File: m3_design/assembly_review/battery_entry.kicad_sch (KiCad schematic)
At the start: 28 parts, among them J1 BAT+ / GND / SW / SW, U9 TPS259470LRPWR

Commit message: R10: m3_design/r10_build.sh and per-family stage gate; m3_design/assembly_review rebuilt as M3-ASSY-R10 (board 883d2db5..., 46 x 90 mm); tools/check.sh passes at zero; binding note bound to the board
Co-Authored-By: Claude Opus 5.5 <noreply@anthropic.com>
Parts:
- added J400: BM02B-GHS-TBT(LF)(SN), rocket:M3_GH_BM02B_GHS_TBT, symbol M3:Conn_1x2
- J1: value BAT+ / GND / SW / SW -> DB125-3.5-2P-GN-S; footprint rocket:M3_DB128V_4P_Entry -> rocket:M3_DB125_2P_GN; symbol M3:BatteryTerminal -> M3:Conn_1x2; LCSC C2915641 -> C466970; Manufacturer Part DB128V-5.08-4P-GN-S -> DB125-3.5-2P-GN-S
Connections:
- net BAT_SW_RETURN: now also J400.2; no longer J1.4 (SW RETURN)
- net BAT_SW_SOURCE: now also J400.1; no longer J1.3 (SW SOURCE)
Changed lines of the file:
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@@
 		(title "07 | Battery input, contact and protection")
 		(date "2026-09-07")
-		(rev "M3-ASSY-R9")
+		(rev "M3-ASSY-R10")
 		(company "Single-board M3 candidate; full system incomplete"))
 	(text "07 | Battery input, contact and protection"
@@
 			(font
 				(size 2.54 2.54))
-			(justify left))
-)
-	(symbol
-		(lib_id "M3:BatteryTerminal")
-		(at 71.12 71.12 0)
-		(unit 1)
-		(in_bom yes)
-		(on_board yes)
-		(dnp no)
-		(property "Reference" "J1"
-			(at 71.12 62.23 0)
-			(effects
-				(font
-					(size 1.27 1.27))))
-		(property "Value" "BAT+ / GND / SW / SW"
-			(at 71.12 66.03999999999999 0)
-			(effects
-				(font
-					(size 1.27 1.27))))
-		(property "Footprint" "rocket:M3_DB128V_4P_Entry"
-			(at 71.12 71.12 0)
-			(hide yes)
-			(effects
-				(font
-					(size 1.27 1.27))))
-		(property "Datasheet" ""
-			(at 71.12 71.12 0)
-			(hide yes)
-			(effects
-				(font
-					(size 1.27 1.27))))
-		(property "LCSC" "C2915641"
-			(at 71.12 71.12 0)
-			(hide yes)
-			(effects
-				(font
-					(size 1.27 1.27))))
-		(property "Manufacturer" "DORABO"
-			(at 71.12 71.12 0)
-			(hide yes)
-			(effects
-				(font
-					(size 1.27 1.27))))
-		(property "Manufacturer Part" "DB128V-5.08-4P-GN-S"
-			(at 71.12 71.12 0)
-			(hide yes)
-			(effects
-				(font
-					(size 1.27 1.27))))
-		(instances
-			(project "m3"
-				(path "/6007a7db-6a58-5660-8beb-956dea045ff8/69ee5338-a377-5d7b-bbd8-28b781c5d2c5"
-					(reference "J1")
-					(unit 1)))))
-	(wire
-		(pts
-			(xy 45.72 69.85)
-			(xy 40.64 69.85))
-		(stroke
-			(width 0)
-			(type default))
-)
-	(global_label "BAT_IN"
-		(shape passive)
-		(at 40.64 69.85 0)
-		(effects
-			(font
-				(size 1.05 1.05))
-			(justify right))
-)
-	(wire
-		(pts
-			(xy 45.72 72.39)
-			(xy 40.64 72.39))
-		(stroke
-			(width 0)
-			(type default))
-)
-	(global_label "GND"
-		(shape passive)
-		(at 40.64 72.39 0)
-		(effects
-			(font
-				(size 1.05 1.05))
-			(justify right))
-)
-	(wire
-		(pts
-			(xy 96.52 69.85)
-			(xy 101.6 69.85))
-		(stroke
-			(width 0)
-			(type default))
-)
-	(global_label "BAT_SW_SOURCE"
-		(shape passive)
-		(at 101.6 69.85 180)
-		(effects
-			(font
-				(size 1.05 1.05))
-			(justify left))
-)
-	(wire
-		(pts
-			(xy 96.52 72.39)
-			(xy 101.6 72.39))
-		(stroke
-			(width 0)
-			(type default))
-)
-	(global_label "BAT_SW_RETURN"
-		(shape passive)
-		(at 101.6 72.39 180)
-		(effects
-			(font
-				(size 1.05 1.05))
 			(justify left))
 )
@@
 		(effects
 			(font
+				(size 1.05 1.05))
+			(justify right))
+)
+	(symbol
+		(lib_id "M3:Conn_1x2")
+		(at 71.12 71.12 0)
+		(unit 1)
+		(in_bom yes)
+		(on_board yes)
+		(dnp no)
+		(property "Reference" "J1"
+			(at 73.66 69.85 0)
+			(effects
+				(font
+					(size 1.27 1.27))
+				(justify left)))
+		(property "Value" "DB125-3.5-2P-GN-S"
+			(at 73.66 72.39 0)
+			(effects
+				(font
+					(size 1.27 1.27))
+				(justify left)))
+		(property "Footprint" "rocket:M3_DB125_2P_GN"
+			(at 71.12 71.12 0)
+			(hide yes)
+			(effects
+				(font
+					(size 1.27 1.27))
+				(justify left)))
+		(property "Datasheet" "https://atta.szlcsc.com/upload/public/pdf/source/20251124/8C215F69B14C8E54AE0F8E5023D4AE9F.pdf"
+			(at 71.12 71.12 0)
+			(hide yes)
+			(effects
+				(font
+					(size 1.27 1.27))
+				(justify left)))
+		(property "LCSC" "C466970"
+			(at 71.12 71.12 0)
+			(hide yes)
+			(effects
+				(font
+					(size 1.27 1.27))
+				(justify left)))
+		(property "Manufacturer" "DORABO"
+			(at 71.12 71.12 0)
+			(hide yes)
+			(effects
+				(font
+					(size 1.27 1.27))
+				(justify left)))
+		(property "Manufacturer Part" "DB125-3.5-2P-GN-S"
+			(at 71.12 71.12 0)
+			(hide yes)
+			(effects
+				(font
+					(size 1.27 1.27))
+				(justify left)))
+		(instances
+			(project "m3"
+				(path "/6007a7db-6a58-5660-8beb-956dea045ff8/69ee5338-a377-5d7b-bbd8-28b781c5d2c5"
+					(reference "J1")
+					(unit 1)))))
+	(wire
+		(pts
+			(xy 63.5 69.85)
+			(xy 58.42 69.85))
+		(stroke
+			(width 0)
+			(type default))
+)
+	(global_label "BAT_IN"
+		(shape passive)
+		(at 58.42 69.85 0)
+		(effects
+			(font
+				(size 1.05 1.05))
+			(justify right))
+)
+	(wire
+		(pts
+			(xy 63.5 72.39)
+			(xy 58.42 72.39))
+		(stroke
+			(width 0)
+			(type default))
+)
+	(global_label "GND"
+		(shape passive)
+		(at 58.42 72.39 0)
+		(effects
+			(font
+				(size 1.05 1.05))
+			(justify right))
+)
+	(symbol
+		(lib_id "M3:Conn_1x2")
+		(at 330.2 238.76 0)
+		(unit 1)
+		(in_bom yes)
+		(on_board yes)
+		(dnp no)
+		(property "Reference" "J400"
+			(at 332.74 237.49 0)
+			(effects
+				(font
+					(size 1.27 1.27))
+				(justify left)))
+		(property "Value" "BM02B-GHS-TBT(LF)(SN)"
+			(at 332.74 240.03 0)
+			(effects
+				(font
+					(size 1.27 1.27))
+				(justify left)))
+		(property "Footprint" "rocket:M3_GH_BM02B_GHS_TBT"
+			(at 330.2 238.76 0)
+			(hide yes)
+			(effects
+				(font
+					(size 1.27 1.27))
+				(justify left)))
+		(property "Datasheet" "https://www.jst-mfg.com/product/pdf/eng/eGH.pdf"
+			(at 330.2 238.76 0)
+			(hide yes)
+			(effects
+				(font
+					(size 1.27 1.27))
+				(justify left)))
+		(property "LCSC" "C161690"
+			(at 330.2 238.76 0)
+			(hide yes)
+			(effects
+				(font
+					(size 1.27 1.27))
+				(justify left)))
+		(property "Manufacturer" "JST"
+			(at 330.2 238.76 0)
+			(hide yes)
+			(effects
+				(font
+					(size 1.27 1.27))
+				(justify left)))
+		(property "Manufacturer Part" "BM02B-GHS-TBT(LF)(SN)"
+			(at 330.2 238.76 0)
+			(hide yes)
+			(effects
+				(font
+					(size 1.27 1.27))
+				(justify left)))
+		(instances
+			(project "m3"
+				(path "/6007a7db-6a58-5660-8beb-956dea045ff8/69ee5338-a377-5d7b-bbd8-28b781c5d2c5"
+					(reference "J400")
+					(unit 1)))))
+	(wire
+		(pts
+			(xy 322.58 237.49)
+			(xy 317.5 237.49))
+		(stroke
+			(width 0)
+			(type default))
+)
+	(global_label "BAT_SW_SOURCE"
+		(shape passive)
+		(at 317.5 237.49 0)
+		(effects
+			(font
+				(size 1.05 1.05))
+			(justify right))
+)
+	(wire
+		(pts
+			(xy 322.58 240.03)
+			(xy 317.5 240.03))
+		(stroke
+			(width 0)
+			(type default))
+)
+	(global_label "BAT_SW_RETURN"
+		(shape passive)
+		(at 317.5 240.03 0)
+		(effects
+			(font

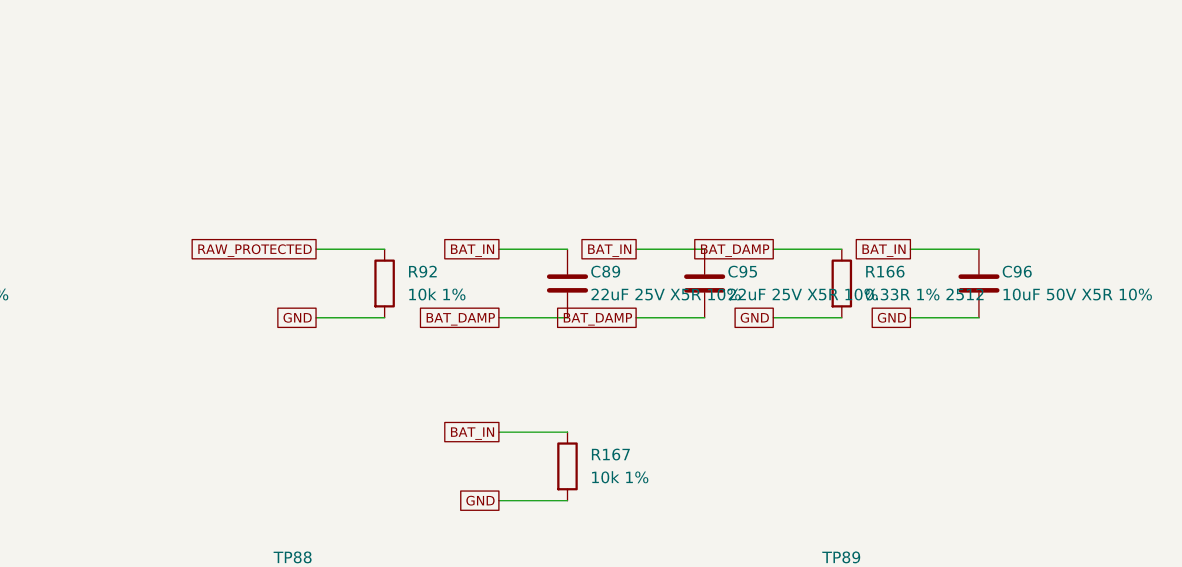
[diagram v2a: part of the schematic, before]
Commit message: R10 owner answers implemented (OQ-1/2/4/5/6/7); single-switch and audit-cut decisions recorded
OQ-2 hot-plug re-modelled on R10's extracted feed (tools/r10_hotplug.py, hotplug.md), damper R166 0.36 ohm
(C168925), F9-1 retargeted to the model; OQ-1 P-11 floor 4.95 mm; OQ-5 firmware load shedding, no hardware cutoff;
OQ-6 no battery-lead fuse (J1 fuse legend removed); OQ-7 board forward of joint +47 mm; OQ-4 aft-edge tab and panel
rail in ORDERING. R10_DECISIONS: requirements-audit cuts AUD-1..10 / GAP-1..5 and the owner's single screw switch
decision (to be implemented next). Board b860afbe..., 46 x 90 mm; two rebuilds byte-identical (agent);
tools/check.sh exit 0 (DRC 0, R10 CAD contract OK, routing hygiene OK, actuator safety contract OK, fab manifest OK).

Co-Authored-By: Claude Opus 5.5 <noreply@anthropic.com>
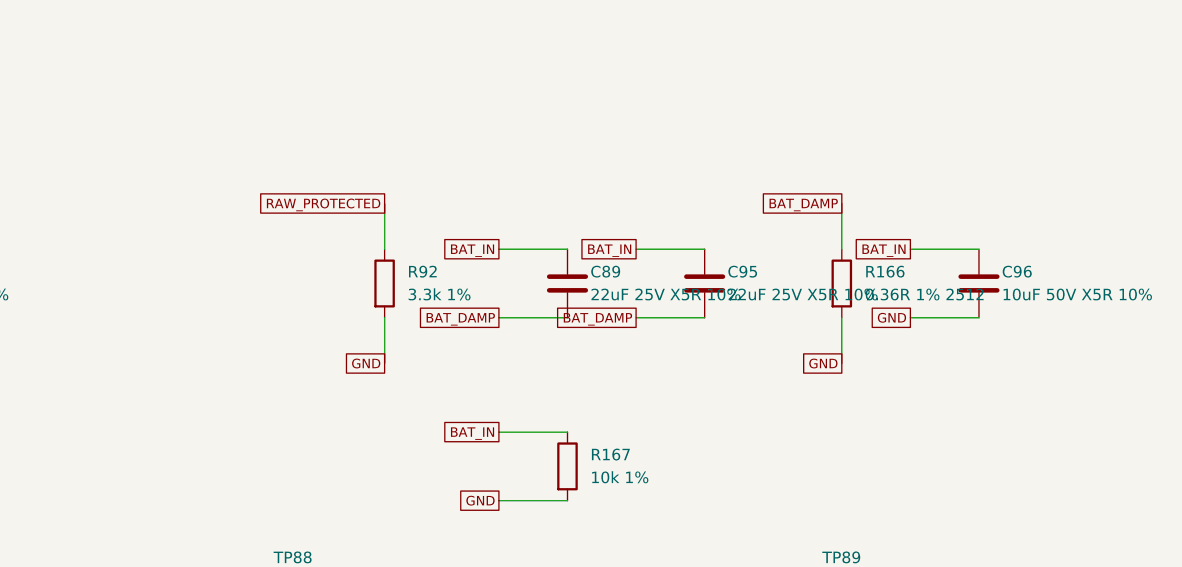
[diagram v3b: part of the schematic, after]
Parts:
- R166: value 0.33R 1% 2512 -> 0.36R 1% 2512; LCSC C25468 -> C168925; LCSC Part C25468 -> (none); Manufacturer Part 25121WF330LT4E -> 25121WF360LT4E
- R92: value 10k 1% -> 3.3k 1%; LCSC C25804 -> C22978; LCSC Part C25804 -> (none); Manufacturer Part 0603WAF1002T5E -> 0603WAF3301T5E

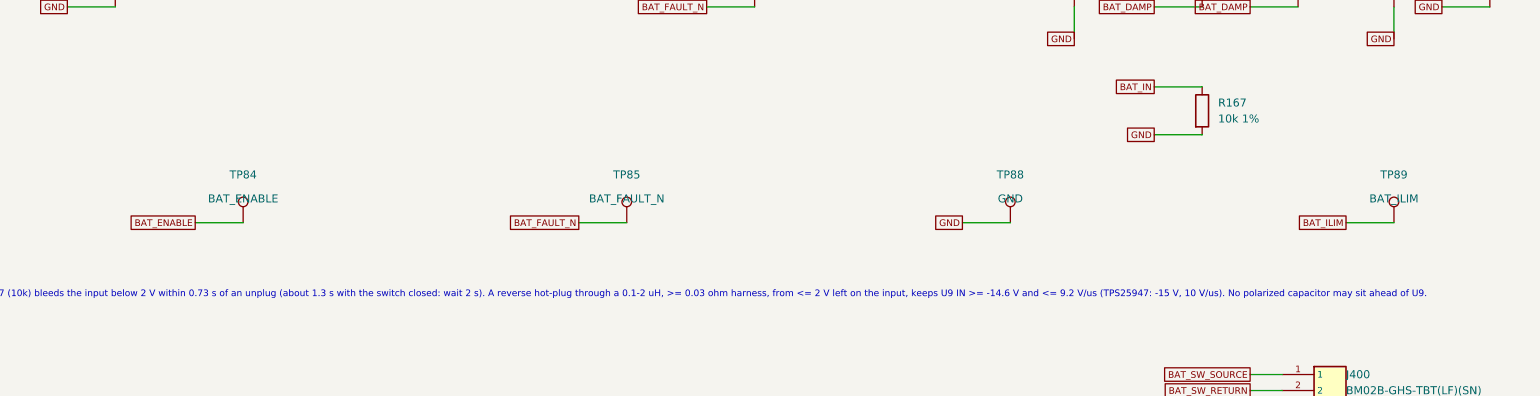
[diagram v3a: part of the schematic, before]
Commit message: R10 requirements-audit cuts and GAP fixes before review round 9
Implement adopted AUD-1 through AUD-10 and GAP-1 through GAP-5 after the single-switch pass.
Remove the advisory pull-pin, redundant probes and GPS/radio IO LDO cells; qualify the smaller
AONR21357 pair, correct C120 voltage rating, standardize shared-code capacitor lands, simplify
slow returns and fire-only copper, localize U9 output protection and add exactly two U401 VIPPO vias.
Record physical-current timing, coupled fire/source budget, C84 manual fitting and narrowed gate scopes.

Board SHA-256: 877d01996a59e9dd5c6dbc367274bb9a323a13982d67960fe46df9b0ee53205d
Board: 46 x 90 mm, 4 layers, 2365477 bytes; 225 footprints, 883 straight tracks, 323 vias.
Netlist SHA-256: 0843da709e2d7a757e9b35cdff48158a54012c5353619cbf409ab961efd2c3ca
Two fresh complete passing builds are byte-identical. Schematic: 700 pins; 22 seeded faults detected.

Final unskipped tools/check.sh: exit 0
DRC violations 0  unconnected 0  schematic parity 0  ERC 0
metadata / 3D model audit: OK
silkscreen outside the board outline: 0 stroke points
fit check: OK (CAD envelopes only)
R10 CAD contract (full): OK
routing hygiene: 0 failing, 0 allowlisted, 0 leftovers recorded
actuator safety contract: OK
Fab manifest: OK; 5 outputs match current CAD and export inputs
Self-tests: shell 4, fit 24, paste 5, routing 59, R10 131; three NumPy cases rerun and passed.

Fab: 215 CPL rows, 82 BOM codes; orientation / paste / manifest pass. Hot-plug: 2304 required
cases plus convergence and controls pass (simulation / Inference). Plate f1 280.9 Hz (Inference).
Live JLC: $84.43 vs $84.41 target, 46 Extended codes; R430 / U4 short. Procurement exit 1 is a
disclosed OQ-3 / ordering deviation, not a CAD gate pass. No quote accepted or order placed.
Firmware, bench, thermal/transient correlation, process acceptance, installed RF immunity and physical fit unverified.

This preparatory pass earns no clean-review credit. Start fresh full ten-lens round 9 on th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
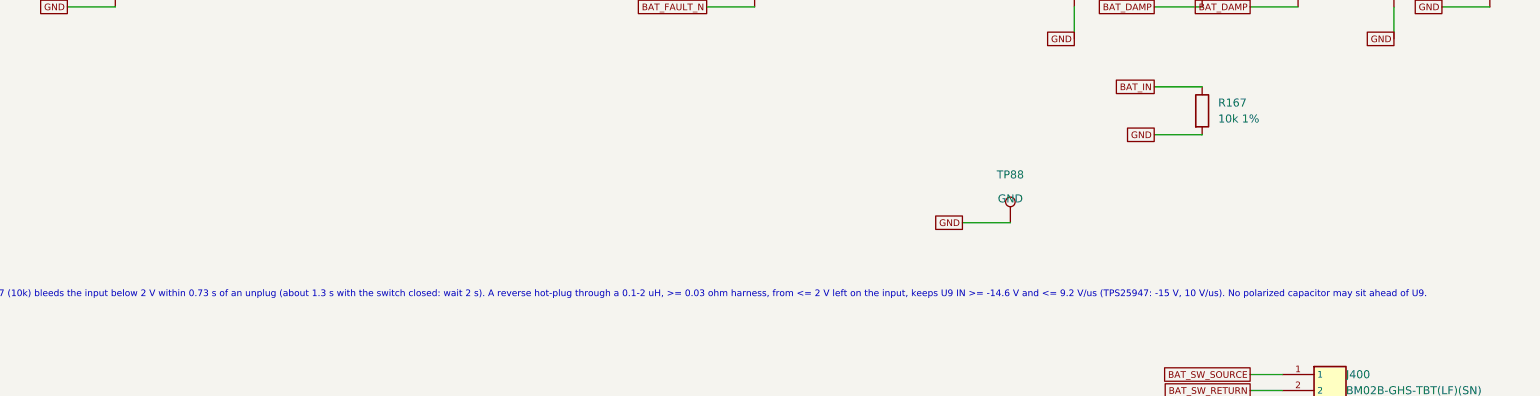
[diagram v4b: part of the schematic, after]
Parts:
- removed TP84: BAT_ENABLE, rocket:M3_TestPad_1.5, symbol M3:TestPoint
- removed TP85: BAT_FAULT_N, rocket:M3_TestPad_1.5, symbol M3:TestPoint
- removed TP89: BAT_ILIM, rocket:M3_TestPad_1.5, symbol M3:TestPoint
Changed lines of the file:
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@@
-	(symbol
-		(lib_id "M3:TestPoint")
-		(at 157.48 213.36 0)
-		(unit 1)
-		(in_bom no)
-		(on_board yes)
-		(dnp no)
-		(property "Reference" "TP84"
-			(at 157.48 205.74 0)
-			(effects
-				(font
-					(size 1.27 1.27))))
-		(property "Value" "BAT_ENABLE"
-			(at 157.48 209.55 0)
-			(effects
-				(font
-					(size 1.27 1.27))))
-		(property "Footprint" "rocket:M3_TestPad_1.5"
-			(at 157.48 213.36 0)
-			(hide yes)
-			(effects
-				(font
-					(size 1.27 1.27))))
-		(property "Datasheet" ""
-			(at 157.48 213.36 0)
-			(hide yes)
-			(effects
-				(font
-					(size 1.27 1.27))))
-		(property "LCSC" ""
-			(at 157.48 213.36 0)
-			(hide yes)
-			(effects
-				(font
-					(size 1.27 1.27))))
-		(instances
-			(project "m3"
-				(path "/6007a7db-6a58-5660-8beb-956dea045ff8/69ee5338-a377-5d7b-bbd8-28b781c5d2c5"
-					(reference "TP84")
-					(unit 1)))))
-	(wire
-		(pts
-			(xy 157.48 213.36)
-			(xy 149.85999999999999 213.36))
-		(stroke
-			(width 0)
-			(type default))
-)
-	(global_label "BAT_ENABLE"
-		(shape passive)
-		(at 149.85999999999999 213.36 0)
-		(effects
-			(font
-				(size 1.05 1.05))
-			(justify right))
-)
-	(symbol
-		(lib_id "M3:TestPoint")
-		(at 218.44 213.36 0)
-		(unit 1)
-		(in_bom no)
-		(on_board yes)
-		(dnp no)
-		(property "Reference" "TP85"
-			(at 218.44 205.74 0)
-			(effects
-				(font
-					(size 1.27 1.27))))
-		(property "Value" "BAT_FAULT_N"
-			(at 218.44 209.55 0)
-			(effects
-				(font
-					(size 1.27 1.27))))
-		(property "Footprint" "rocket:M3_TestPad_1.5"
-			(at 218.44 213.36 0)
-			(hide yes)
-			(effects
-				(font
-					(size 1.27 1.27))))
-		(property "Datasheet" ""
-			(at 218.44 213.36 0)
-			(hide yes)
-			(effects
-				(font
-					(size 1.27 1.27))))
-		(property "LCSC" ""
-			(at 218.44 213.36 0)
-			(hide yes)
-			(effects
-				(font
-					(size 1.27 1.27))))
-		(instances
-			(project "m3"
-				(path "/6007a7db-6a58-5660-8beb-956dea045ff8/69ee5338-a377-5d7b-bbd8-28b781c5d2c5"
-					(reference "TP85")
-					(unit 1)))))
-	(wire
-		(pts
-			(xy 218.44 213.36)
-			(xy 210.82 213.36))
-		(stroke
-			(width 0)
-			(type default))
-)
-	(global_label "BAT_FAULT_N"
-		(shape passive)
-		(at 210.82 213.36 0)
-		(effects
-			(font
-				(size 1.05 1.05))
-			(justify right))
-)
 	(symbol
 		(lib_id "M3:TestPoint")
@@
 		(effects
 			(font
-				(size 1.05 1.05))
-			(justify right))
-)
-	(symbol
-		(lib_id "M3:TestPoint")
-		(at 340.36 213.36 0)
-		(unit 1)
-		(in_bom no)
-		(on_board yes)
-		(dnp no)
-		(property "Reference" "TP89"
-			(at 340.36 205.74 0)
-			(effects
-				(font
-					(size 1.27 1.27))))
-		(property "Value" "BAT_ILIM"
-			(at 340.36 209.55 0)
-			(effects
-				(font
-					(size 1.27 1.27))))
-		(property "Footprint" "rocket:M3_TestPad_1.5"
-			(at 340.36 213.36 0)
-			(hide yes)
-			(effects
-				(font
-					(size 1.27 1.27))))
-		(property "Datasheet" ""
-			(at 340.36 213.36 0)
-			(hide yes)
-			(effects
-				(font
-					(size 1.27 1.27))))
-		(property "LCSC" ""
-			(at 340.36 213.36 0)
-			(hide yes)
-			(effects
-				(font
-					(size 1.27 1.27))))
-		(instances
-			(project "m3"
-				(path "/6007a7db-6a58-5660-8beb-956dea045ff8/69ee5338-a377-5d7b-bbd8-28b781c5d2c5"
-					(reference "TP89")
-					(unit 1)))))
-	(wire
-		(pts
-			(xy 340.36 213.36)
-			(xy 332.74 213.36))
-		(stroke
-			(width 0)
-			(type default))
-)
-	(global_label "BAT_ILIM"
-		(shape passive)
-		(at 332.74 213.36 0)
-		(effects
-			(font
